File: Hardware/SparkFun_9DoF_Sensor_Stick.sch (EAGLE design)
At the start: 34 parts, among them U1 ITG-32001:1, U2 ADXL345", U3 3.3V/150mA, U4 HMC5883LSMD

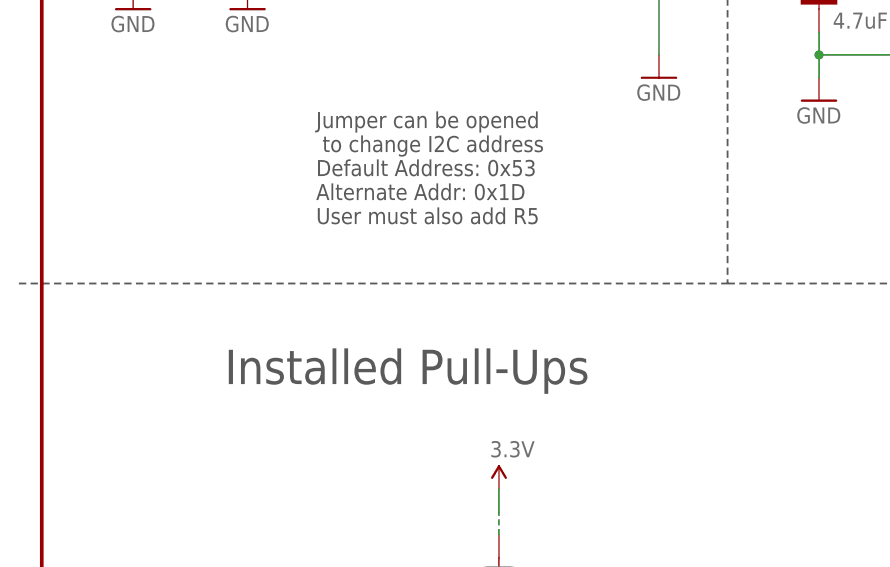
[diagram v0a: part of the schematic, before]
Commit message: Fixing QC issues
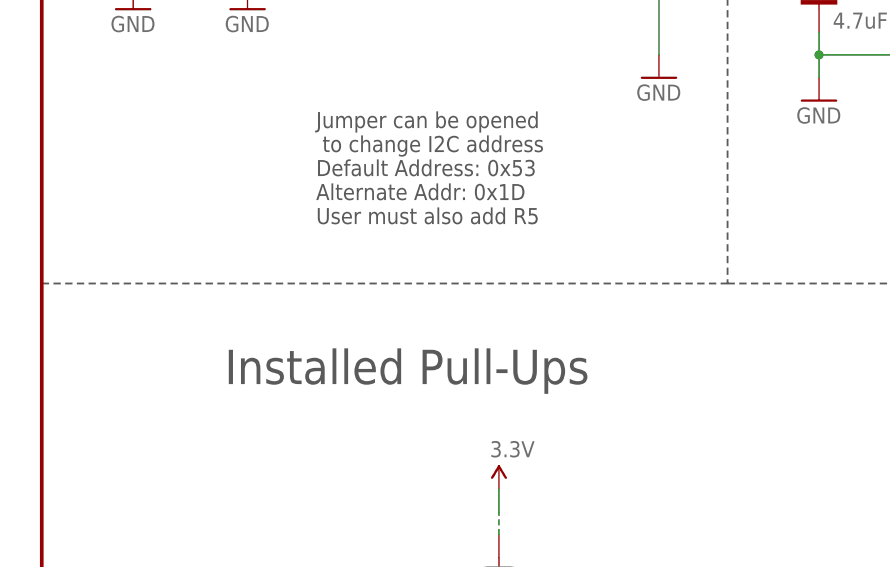
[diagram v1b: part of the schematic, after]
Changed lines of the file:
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@@
 <text x="175.768" y="6.858" size="2.54" layer="94">Toni Klopfenstein</text>
 <text x="236.728" y="6.858" size="2.54" layer="94">v16</text>
-<wire x1="-2.54" y1="96.52" x2="76.2" y2="96.52" width="0.2032" layer="97" style="longdash"/>
+<wire x1="0" y1="96.52" x2="76.2" y2="96.52" width="0.2032" layer="97" style="longdash"/>
 <wire x1="101.6" y1="96.52" x2="157.48" y2="96.52" width="0.2032" layer="97" style="longdash"/>
 <wire x1="157.48" y1="96.52" x2="248.92" y2="96.52" width="0.2032" layer="97" style="longdash"/>

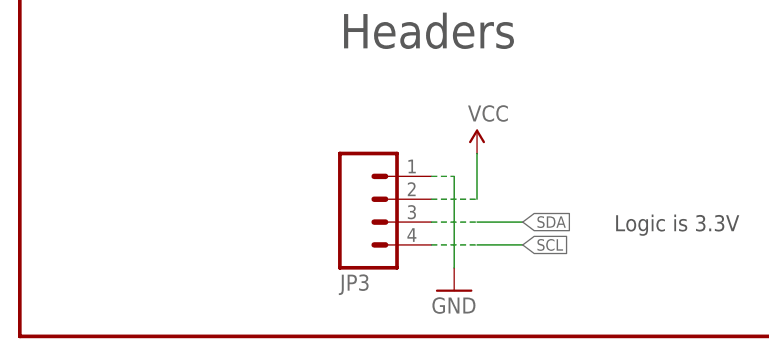
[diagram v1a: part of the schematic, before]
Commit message: Swapping JP1 and JP3 names on parts
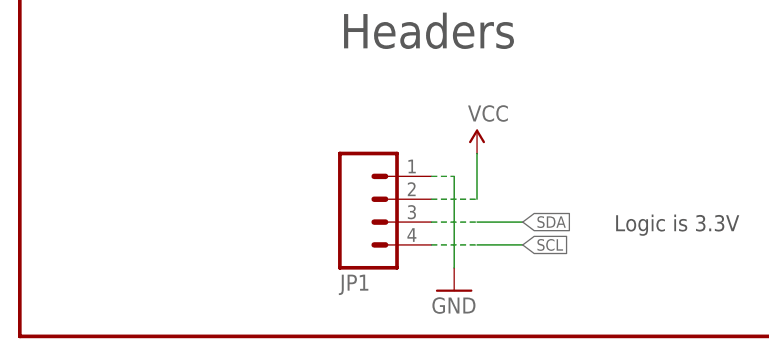
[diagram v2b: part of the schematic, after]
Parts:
- JP1: value FIDUCIALUFIDUCIAL -> (none); device SparkFun-Aesthetics:FIDUCIALUFIDUCIAL -> SparkFun-Connectors:M04PTH
- JP3: value (none) -> FIDUCIALUFIDUCIAL; device SparkFun-Connectors:M04PTH -> SparkFun-Aesthetics:FIDUCIALUFIDUCIAL
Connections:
- net GND: now also JP1.1; no longer JP3.1
- net SCL: now also JP1.4; no longer JP3.4
- net SDA: now also JP1.3; no longer JP3.3
- net VCC: now also JP1.2; no longer JP3.2
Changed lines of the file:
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@@
 <part name="P+6" library="SparkFun-Aesthetics" deviceset="3.3V" device=""/>
 <part name="GND10" library="SparkFun-Aesthetics" deviceset="GND" device=""/>
-<part name="JP3" library="SparkFun-Connectors" deviceset="M04" device="PTH"/>
+<part name="JP1" library="SparkFun-Connectors" deviceset="M04" device="PTH"/>
 <part name="GND11" library="SparkFun-Aesthetics" deviceset="GND" device=""/>
 <part name="C10" library="SparkFun-Capacitors" deviceset="0.1UF-25V(+80/-20%)(0603)" device="" value="0.1uF"/>
@@
 <part name="P+11" library="SparkFun-Aesthetics" deviceset="3.3V" device=""/>
 <part name="GND15" library="SparkFun-Aesthetics" deviceset="GND" device=""/>
-<part name="JP1" library="SparkFun-Aesthetics" deviceset="FIDUCIAL" device="UFIDUCIAL" value="FIDUCIALUFIDUCIAL"/>
+<part name="JP3" library="SparkFun-Aesthetics" deviceset="FIDUCIAL" device="UFIDUCIAL" value="FIDUCIALUFIDUCIAL"/>
 <part name="P+8" library="SparkFun-Aesthetics" deviceset="3.3V" device=""/>
 <part name="JP2" library="SparkFun-Aesthetics" deviceset="FIDUCIAL" device="UFIDUCIAL" value="FIDUCIALUFIDUCIAL"/>
@@
 <instance part="P+6" gate="G$1" x="170.18" y="129.54"/>
 <instance part="GND10" gate="1" x="218.44" y="132.08"/>
-<instance part="JP3" gate="G$1" x="40.64" y="15.24" rot="MR180"/>
+<instance part="JP1" gate="G$1" x="40.64" y="15.24" rot="MR180"/>
 <instance part="GND11" gate="1" x="147.32" y="43.18"/>
 <instance part="C10" gate="G$1" x="198.12" y="58.42"/>
@@
 <instance part="P+11" gate="G$1" x="210.82" y="76.2"/>
 <instance part="GND15" gate="1" x="210.82" y="43.18"/>
-<instance part="JP1" gate="G$1" x="246.38" y="33.02"/>
+<instance part="JP3" gate="G$1" x="246.38" y="33.02"/>
 <instance part="P+8" gate="G$1" x="165.1" y="160.02"/>
 <instance part="JP2" gate="G$1" x="243.84" y="33.02"/>
@@
 <wire x1="48.26" y1="17.78" x2="48.26" y2="7.62" width="0.1524" layer="91"/>
 <pinref part="GND14" gate="1" pin="GND"/>
-<pinref part="JP3" gate="G$1" pin="1"/>
+<pinref part="JP1" gate="G$1" pin="1"/>
 <wire x1="45.72" y1="17.78" x2="48.26" y2="17.78" width="0.1524" layer="91" style="longdash"/>
 </segment>
@@
 <wire x1="50.8" y1="12.7" x2="55.88" y2="12.7" width="0.1524" layer="91"/>
 <label x="55.88" y="12.7" size="1.27" layer="95" xref="yes"/>
-<pinref part="JP3" gate="G$1" pin="3"/>
+<pinref part="JP1" gate="G$1" pin="3"/>
 <wire x1="45.72" y1="12.7" x2="50.8" y2="12.7" width="0.1524" layer="91" style="longdash"/>
 </segment>
@@
 <wire x1="50.8" y1="10.16" x2="55.88" y2="10.16" width="0.1524" layer="91"/>
 <label x="55.88" y="10.16" size="1.27" layer="95" xref="yes"/>
-<pinref part="JP3" gate="G$1" pin="4"/>
+<pinref part="JP1" gate="G$1" pin="4"/>
 <wire x1="45.72" y1="10.16" x2="50.8" y2="10.16" width="0.1524" layer="91" style="longdash"/>
 </segment>
@@
 <wire x1="50.8" y1="20.32" x2="50.8" y2="15.24" width="0.1524" layer="91"/>
 <pinref part="P+10" gate="G$1" pin="VCC"/>
-<pinref part="JP3" gate="G$1" pin="2"/>
+<pinref part="JP1" gate="G$1" pin="2"/>
 <wire x1="45.72" y1="15.24" x2="50.8" y2="15.24" width="0.1524" layer="91" style="longdash"/>
 </segment>
